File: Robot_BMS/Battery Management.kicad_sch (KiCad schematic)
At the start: 27 parts, among them IC2 BQ76922RSNR, Q2 SIS413DN-T1-GE3, Q3 2N7002, Q4 SIS413DN-T1-GE3

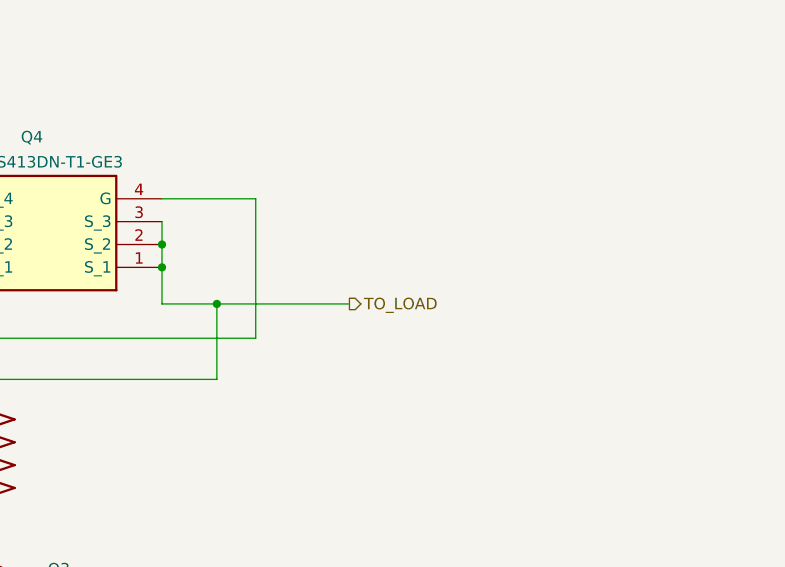
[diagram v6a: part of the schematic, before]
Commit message: switching usb c pd chip to ap33772 due to better support online
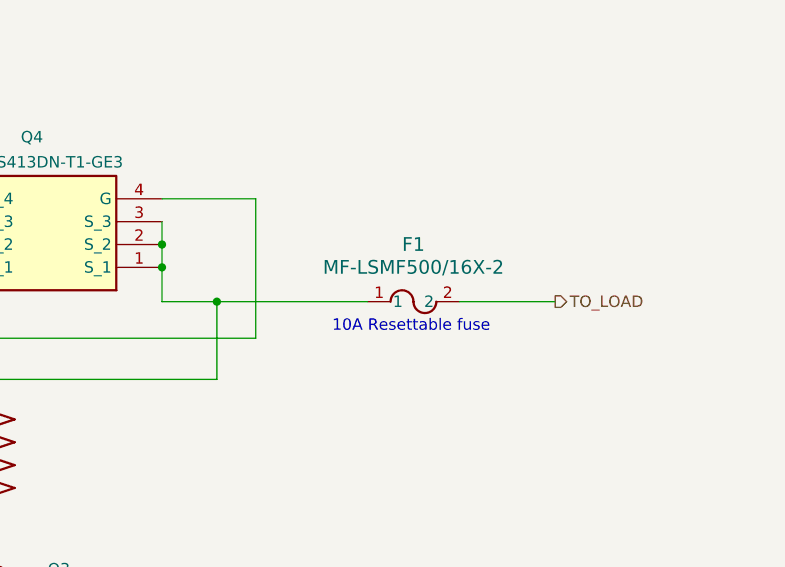
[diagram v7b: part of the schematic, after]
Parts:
- added F1: MF-LSMF500/16X-2, RobotBMS:FUSE_MF-LSMF185&slash_33X_BRN, symbol ul_MF-LSMF500-16X-2:MF-LSMF500_16X-2
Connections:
- net TO_LOAD: now also F1.2; no longer Q4.1 (S_1), Q4.2 (S_2), Q4.3 (S_3), R17.2
- new net: F1.1, Q4.1 (S_1), Q4.2 (S_2), Q4.3 (S_3), R17.2
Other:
- note added: "10A Resettable fuse"
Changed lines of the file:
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@@
 	(paper "A4")
 	(junction
-		(at 192.278 52.578)
-		(diameter 0)
-		(color 0 0 0 0)
-	)
-	(junction
 		(at 115.316 177.038)
 		(diameter 0)
@@
 	(junction
 		(at 109.728 98.806)
+		(diameter 0)
+		(color 0 0 0 0)
+	)
+	(junction
+		(at 192.278 52.324)
 		(diameter 0)
 		(color 0 0 0 0)
@@
 	(wire
 		(pts
-			(xy 186.182 52.578) (xy 192.278 52.578)
+			(xy 186.182 52.324) (xy 192.278 52.324)
 		)
 		(stroke
@@
 		(pts
 			(xy 78.994 123.698) (xy 94.488 123.698)
+		)
+		(stroke
+			(width 0)
+			(type default)
+		)
+	)
+	(wire
+		(pts
+			(xy 219.202 52.324) (xy 229.87 52.324)
 		)
 		(stroke
@@
 	(wire
 		(pts
+			(xy 209.042 52.324) (xy 192.278 52.324)
+		)
+		(stroke
+			(width 0)
+			(type default)
+		)
+	)
+	(wire
+		(pts
 			(xy 112.522 72.136) (xy 117.348 72.136)
 		)
@@
 	(wire
 		(pts
-			(xy 186.182 48.514) (xy 186.182 52.578)
+			(xy 186.182 48.514) (xy 186.182 52.324)
 		)
 		(stroke
@@
 	(wire
 		(pts
+			(xy 192.278 52.324) (xy 192.278 52.578)
+		)
+		(stroke
+			(width 0)
+			(type default)
+		)
+	)
+	(wire
+		(pts
 			(xy 127.508 153.67) (xy 128.778 153.67)
 		)
@@
 		(pts
 			(xy 167.894 78.74) (xy 167.894 79.248)
-		)
-		(stroke
-			(width 0)
-			(type default)
-		)
-	)
-	(wire
-		(pts
-			(xy 192.278 52.578) (xy 207.01 52.578)
 		)
 		(stroke
@@
 		)
 	)
+	(text "10A Resettable fuse\n\n"
+		(exclude_from_sim no)
+		(at 213.868 56.134 0)
+		(effects
+			(font
+				(size 1.27 1.27)
+			)
+		)
+	)
 	(hierarchical_label "GND"
 		(shape output)
@@
 	(hierarchical_label "TO_LOAD"
 		(shape output)
-		(at 207.01 52.578 0)
+		(at 229.87 52.324 0)
 		(effects
 			(font
@@
 					(unit 1)
 				)
+			)
+		)
+	)
+	(symbol
+		(lib_id "ul_MF-LSMF500-16X-2:MF-LSMF500_16X-2")
+		(at 209.042 52.324 0)
+		(unit 1)
+		(exclude_from_sim no)
+		(in_bom yes)
+		(on_board yes)
+		(dnp no)
+		(fields_autoplaced yes)
+		(property "Reference" "F1"
+			(at 214.122 45.974 0)
+			(effects
+				(font
+					(size 1.524 1.524)
+				)
+			)
+		)
+		(property "Value" "MF-LSMF500/16X-2"
+			(at 214.122 48.514 0)
+			(effects
+				(font
+					(size 1.524 1.524)
+				)
+			)
+		)
+		(property "Footprint" "RobotBMS:FUSE_MF-LSMF185&slash_33X_BRN"
+			(at 209.042 52.324 0)
+			(effects
+				(font
+					(size 1.27 1.27)
+					(italic yes)
+				)
+				(hide yes)
+			)
+		)
+		(property "Datasheet" "MF-LSMF500/16X-2"
+			(at 209.042 52.324 0)
+			(effects
+				(font
+					(size 1.27 1.27)
+					(italic yes)
+				)
+				(hide yes)
+			)
+		)
+		(property "Description" ""
+			(at 209.042 52.324 0)
+			(effects
+				(font
+					(size 1.27 1.27)
+				)
+				(hide yes)
+			)
+		)
+		(pin "1"
+		)
+		(pin "2"
+		)
+		(instances
+			(project ""
+				(path "/72551b1c-3d40-4199-8911-e5b015f4abec/26a1c9c5-a214-45fb-a345-5a76cfe84f03"
+					(reference "F1")
+					(unit 1)
+				)

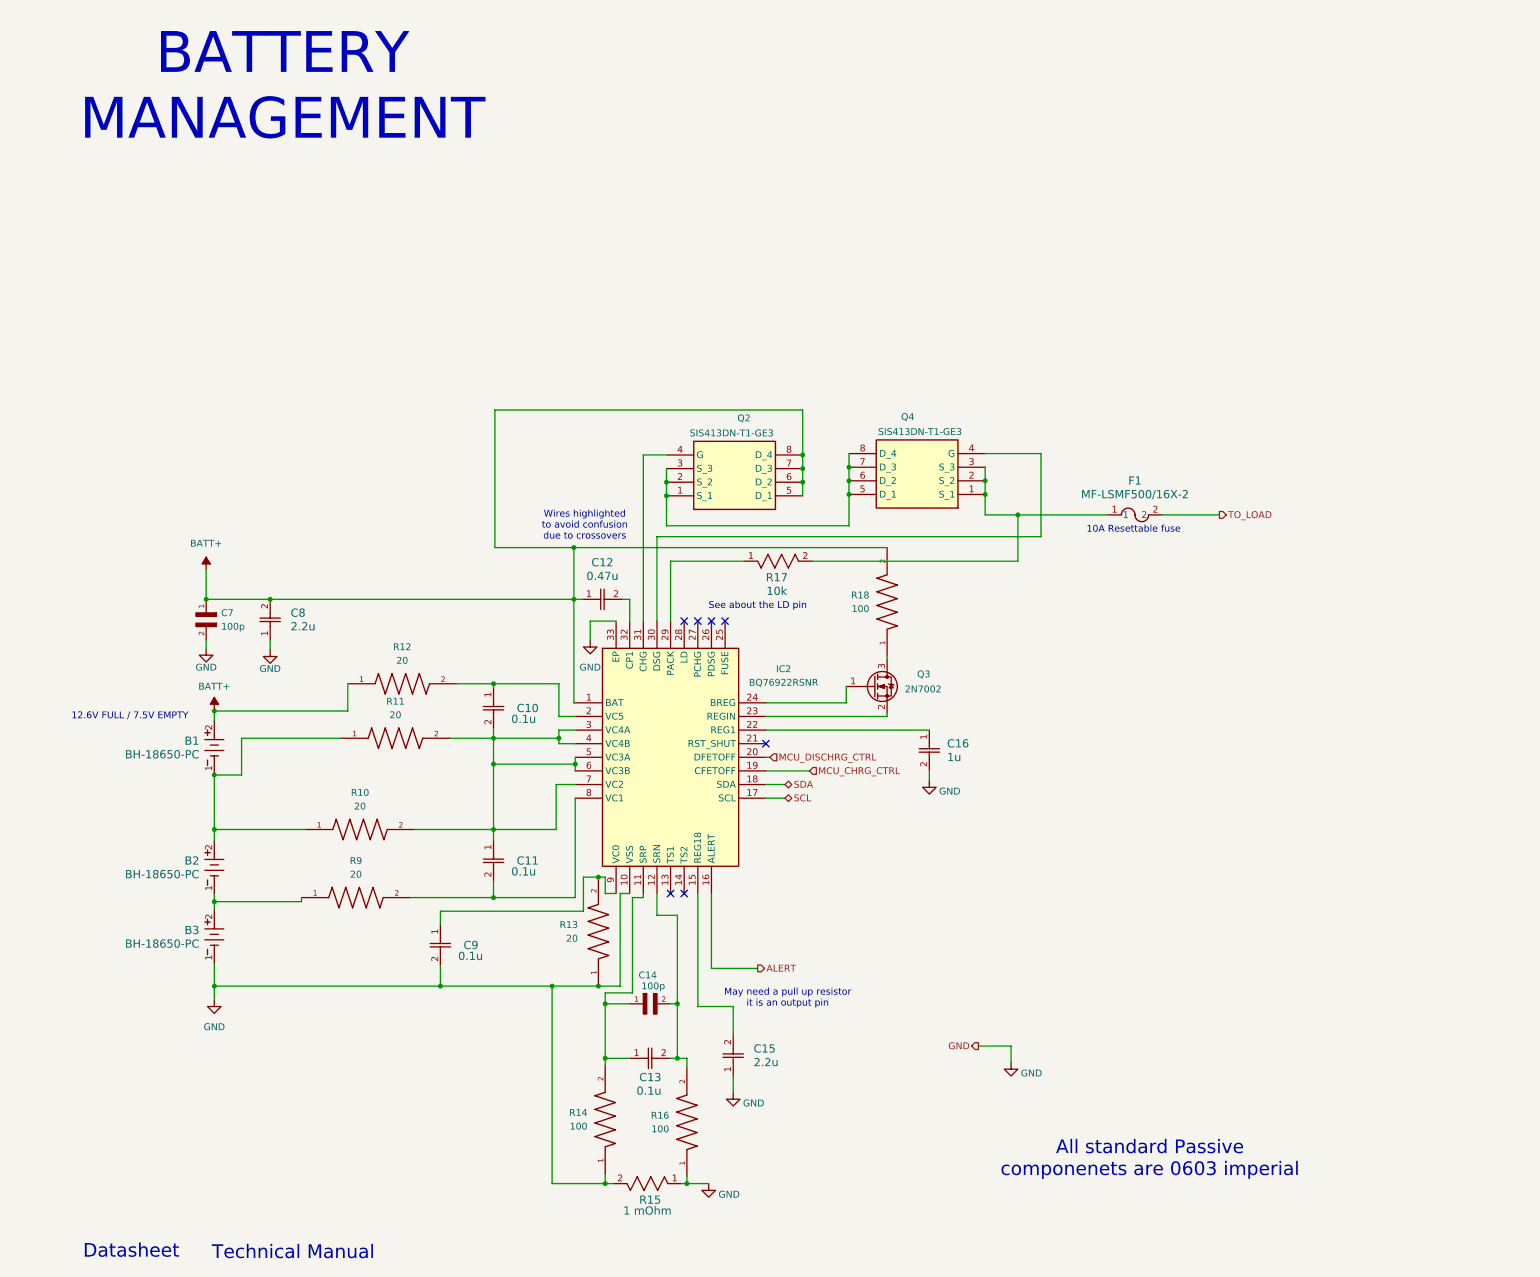
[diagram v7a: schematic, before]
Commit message: placed connectors for BMS PCB
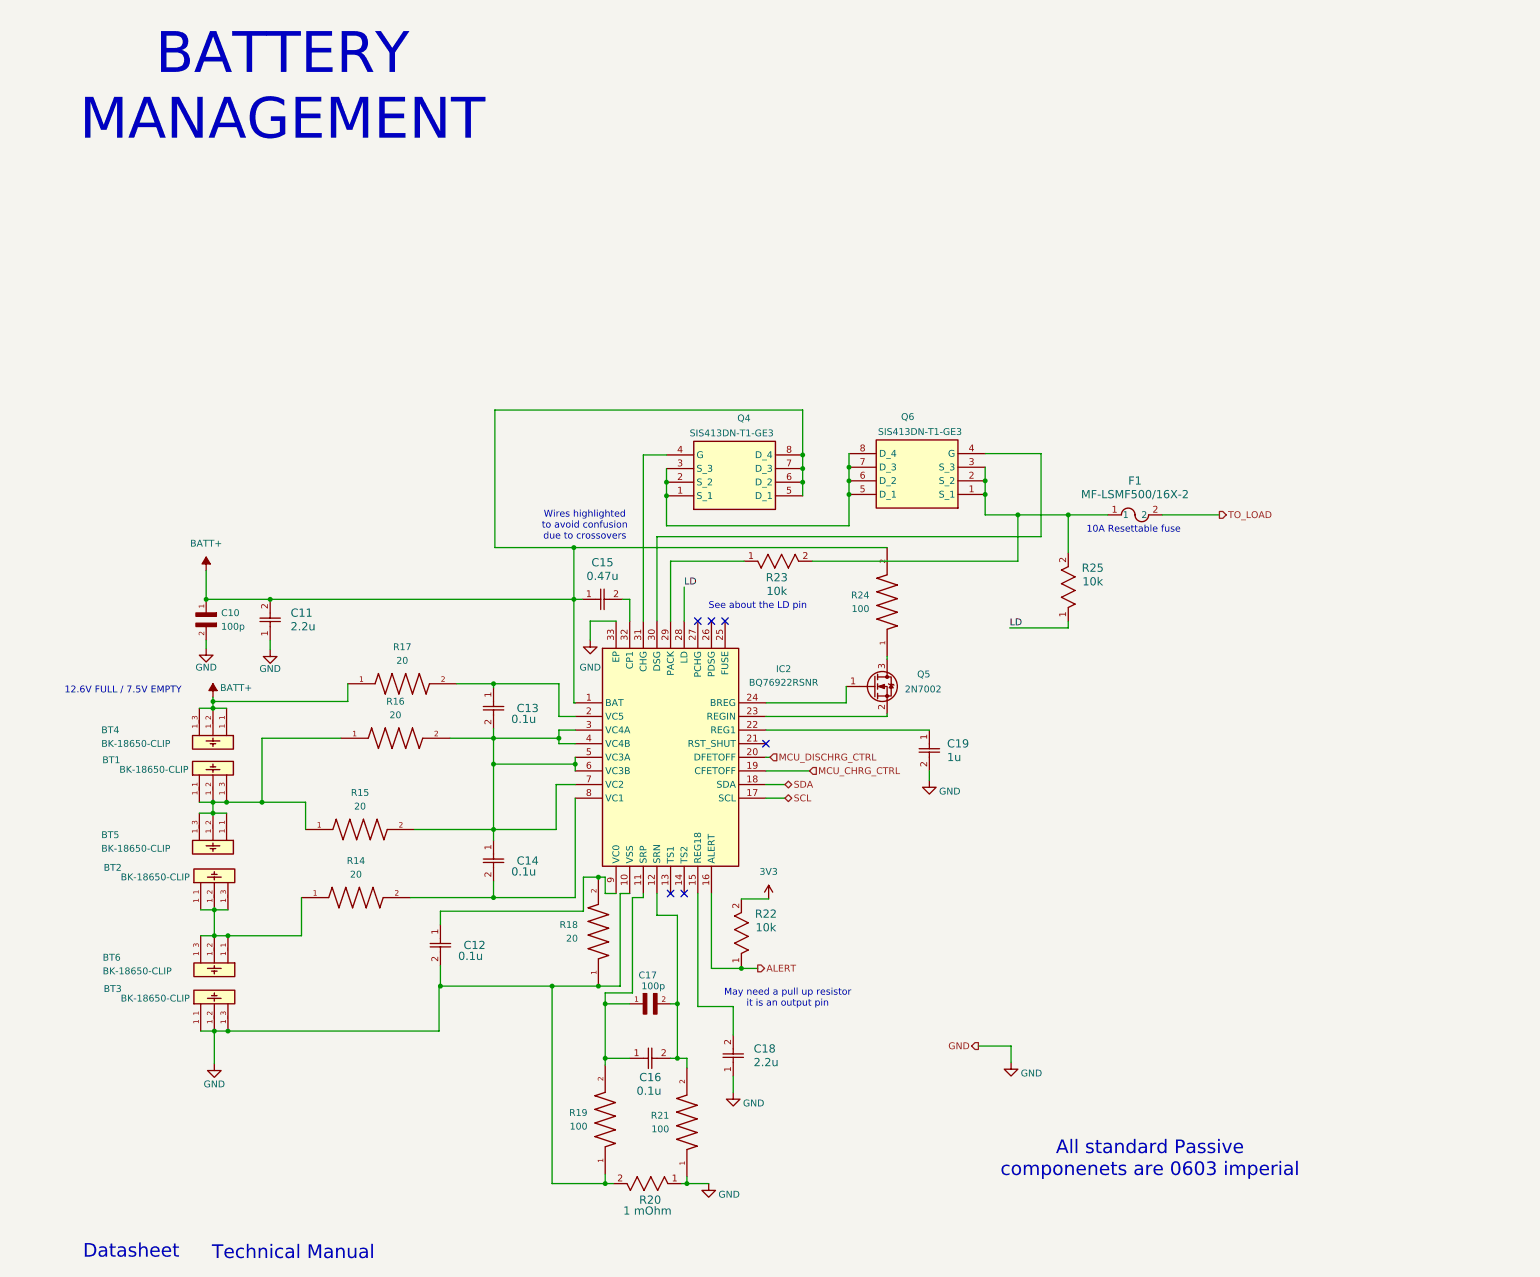
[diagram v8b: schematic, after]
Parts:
- removed B1, B2, B3: BH-18650-PC, RobotBMS:BAT_BH-18650-PC_MPD, symbol 18650 Battery Holder:BH-18650-PC
- added BT1, BT2, BT3, BT4, BT5, BT6: BK-18650-CLIP, RobotBMS:BAT_BK-18650-CLIP, symbol BK-18650-Clip:BK-18650-CLIP
- added R22, R25: 10k, RobotBMS:RC0603N_YAG, symbol RC0603FR-0710KL:RC0603FR-0710KL
- renumbered C7 to C10, C8 to C11, C9 to C12, C10 to C13, C11 to C14, C12 to C15, C13 to C16, C14 to C17, C15 to C18, C16 to C19, Q2 to Q4, Q3 to Q5, Q4 to Q6, R9 to R14, R10 to R15, R11 to R16, R12 to R17, R13 to R18, R14 to R19, R15 to R20, R16 to R21, R17 to R23, R18 to R24
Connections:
- net ALERT: now also R22.1
- net BATT+: now also BT4.1_1, BT4.1_2, BT4.1_3
- net GND: now also BT3.1_1, BT3.1_2, BT3.1_3
- net at F1.1, Q6.1 (S_1), Q6.2 (S_2)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: now also R25.2
- net at R14.1: now also BT2.1_1, BT2.1_2, BT2.1_3, BT6.1_1, BT6.1_2, BT6.1_3
- net LD: now reaches IC2.28 (LD)
- net LD: now also R25.1
- net at R15.1, R16.1: now also BT1.1_1, BT1.1_2, BT1.1_3, BT5.1_1, BT5.1_2, BT5.1_3
- new net 3V3: R22.2
- no-connect marks 7 -> 6
